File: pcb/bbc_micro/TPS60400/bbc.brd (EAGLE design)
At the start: 43 x 30 mm, 24 parts, among them U2 LM2776

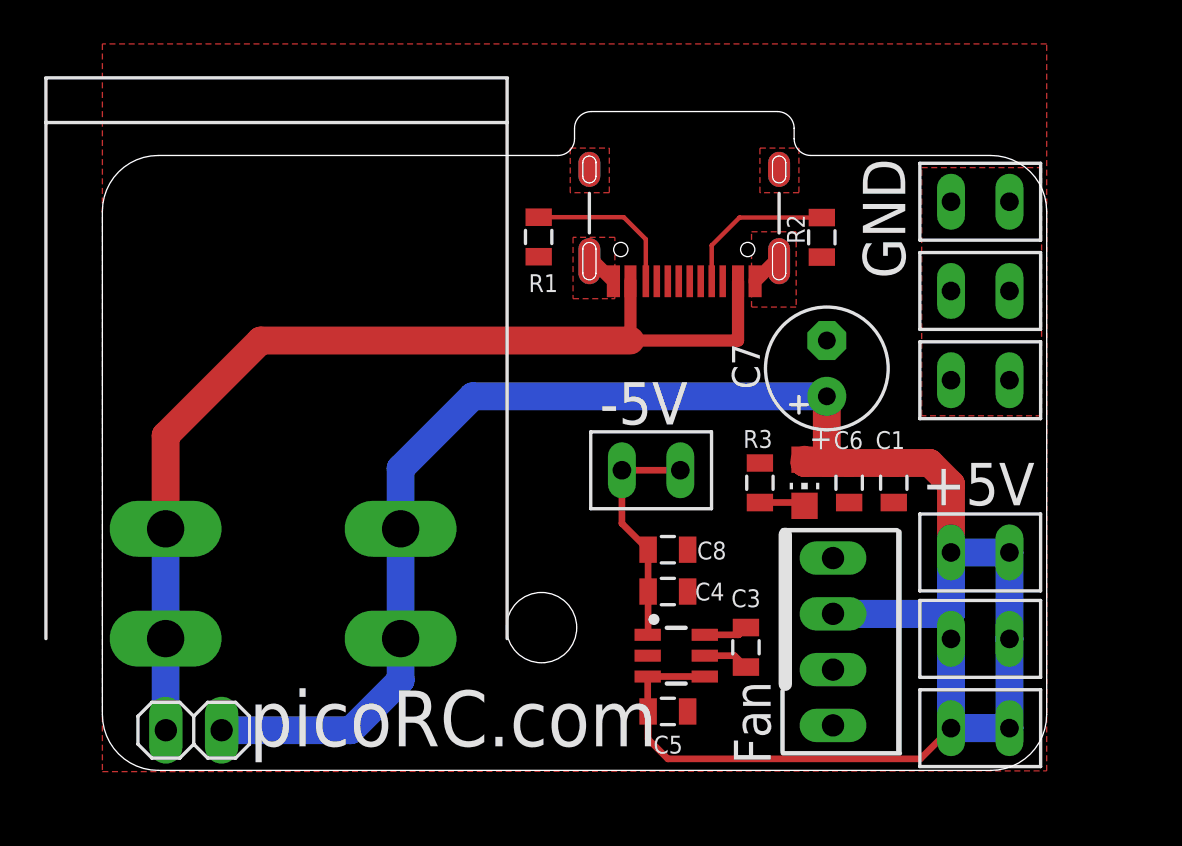
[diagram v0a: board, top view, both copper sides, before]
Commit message: changed bbc micro PCB with LM2776
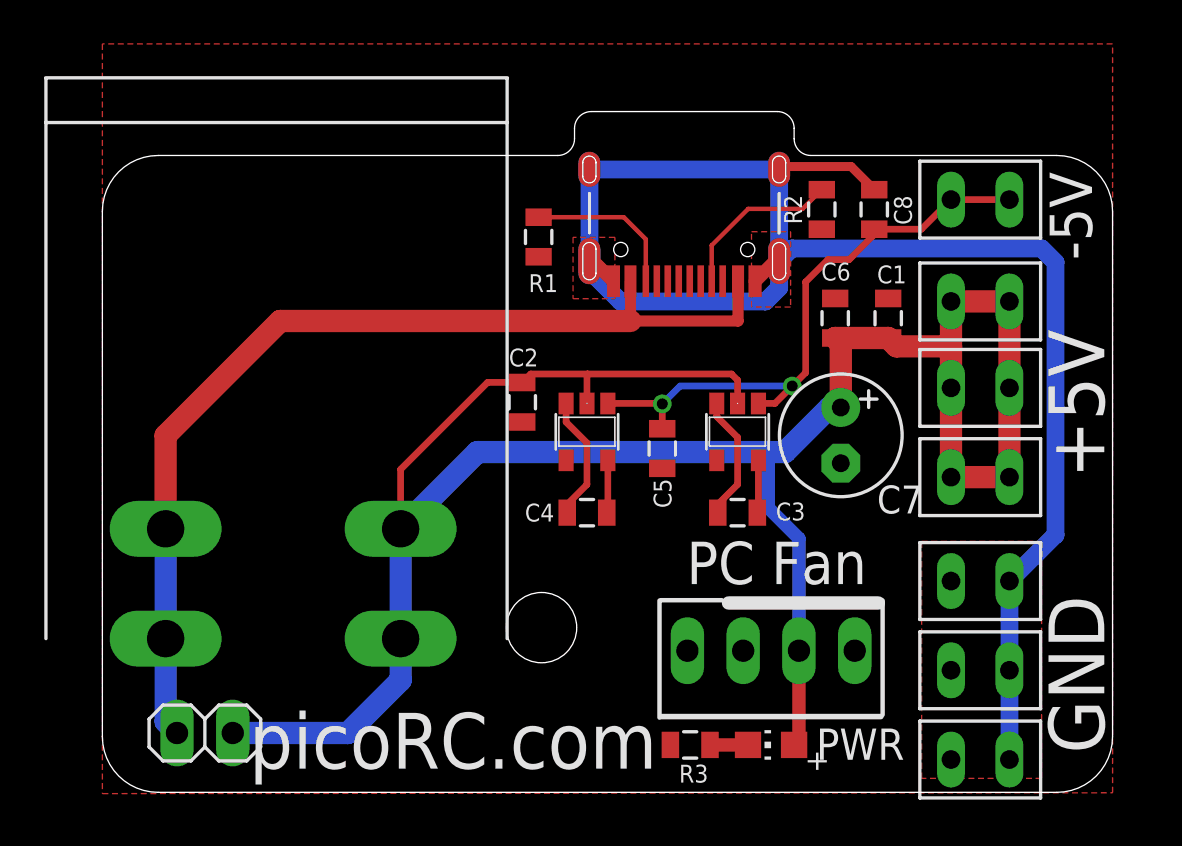
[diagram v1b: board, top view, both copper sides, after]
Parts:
- removed U2: LM2776, dword1511-pmic-dcdc:SOT-23-6
- added C2: 1uF, clock:0805@1
- added U1, U3: TPS60400DVBR, TPS6040x:SOT23-5
- C4: value 2.2uF -> 1uF
- moved U$5 19.4 mm to (46.0, 27.0), turned to 0 degrees
- moved C8 18.1 mm to (41.1, 26.5), turned to 270 degrees
- moved U$10 17.3 mm to (46.0, 5.56)
- moved U$11 17.3 mm to (46.0, 1.49)
- moved U$9 17.3 mm to (46.0, 9.62)
- moved R3 12.4 mm to (32.8, 2.16), turned to 0 degrees
- moved LED3 12.0 mm to (36.4, 2.16), turned to 90 degrees
- moved C5 12.0 mm to (31.5, 15.7), turned to 270 degrees
- moved U$7 11.4 mm to (46.0, 18.4)
- moved U$6 11.4 mm to (46.0, 22.4)
- moved U$8 11.4 mm to (46.0, 14.4)
- moved C6 7.52 mm to (39.4, 21.6), turned to 270 degrees
- moved C1 7.50 mm to (41.8, 21.6), turned to 270 degrees
- moved C3 6.14 mm to (34.9, 12.7), turned to 180 degrees
- moved C4 5.14 mm to (28.1, 12.7), turned to 180 degrees
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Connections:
- new net -5V: C5.1, C8.2, U$5.P$1, U$5.P$2, U1.1, U3.1
- new net N$5: C4.1, U1.5
- net +5V: now also C2.2, U1.2, U3.2; no longer C5.1, U2.3, U2.4
- net GND: now also C2.1, U1.4, U3.4; no longer C4.2, U2.2
- net N$2: now also U3.3; no longer U2.5
- net N$3: now also U3.5; no longer U2.6
- net N$4: now also C4.2, U1.3; no longer C4.1, C8.2, U$5.P$1, U$5.P$2, U2.1
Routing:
- net GND: track 2.95 -> 72.5 mm
- net -5V: track 0.00 -> 27.7 mm, vias 0 -> 2
- net N$4: track 10.7 -> 5.74 mm
- net +5V: track 99.8 -> 104.3 mm
- net N$2: track 2.09 -> 5.74 mm
- net N$5: track 0.00 -> 2.40 mm
- net N$1: track 46.7 -> 45.6 mm
- net N$6: track 7.17 -> 7.70 mm
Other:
- board size 43 x 30 mm -> 46 x 31 mm
- board text added: "PC Fan"
- board text added: "PWR"
- board text removed: "Fan"
